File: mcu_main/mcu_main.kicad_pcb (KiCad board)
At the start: 2 copper layers, 108 x 61.7 mm, 55 parts, among them J1 Micro_SD_Card_Det_Hirose_DM3AT, J10 Conn_01x02_Pin, J2 Conn_01x10_Pin, J3 Conn_01x06_Pin, J4 4P4C_Shielded, J5 4P4C_Shielded, J6 Screw_Terminal_01x03_ebrake, J7 Screw_Terminal_01x03_throttle, J8 Screw_Terminal_01x06, J9 Conn_01x14_Socket, U1 ESP32-S3-WROOM-1, U2 USB_C_connector, U3 SGM2212-3.3, U4 VL53L1CXV0FY1, sw1 SW_Push_Dual, sw2 SW_Push_Dual

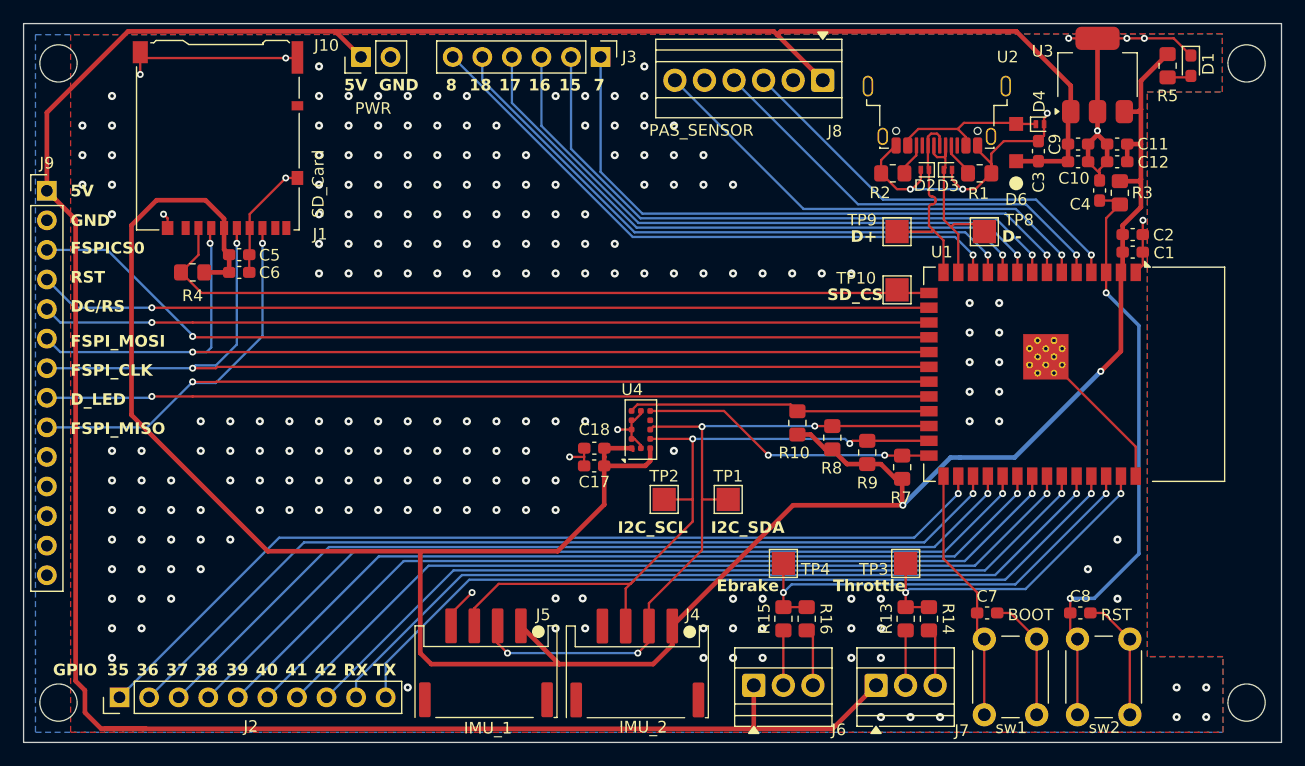
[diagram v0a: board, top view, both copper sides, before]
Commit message: fixed resistor values
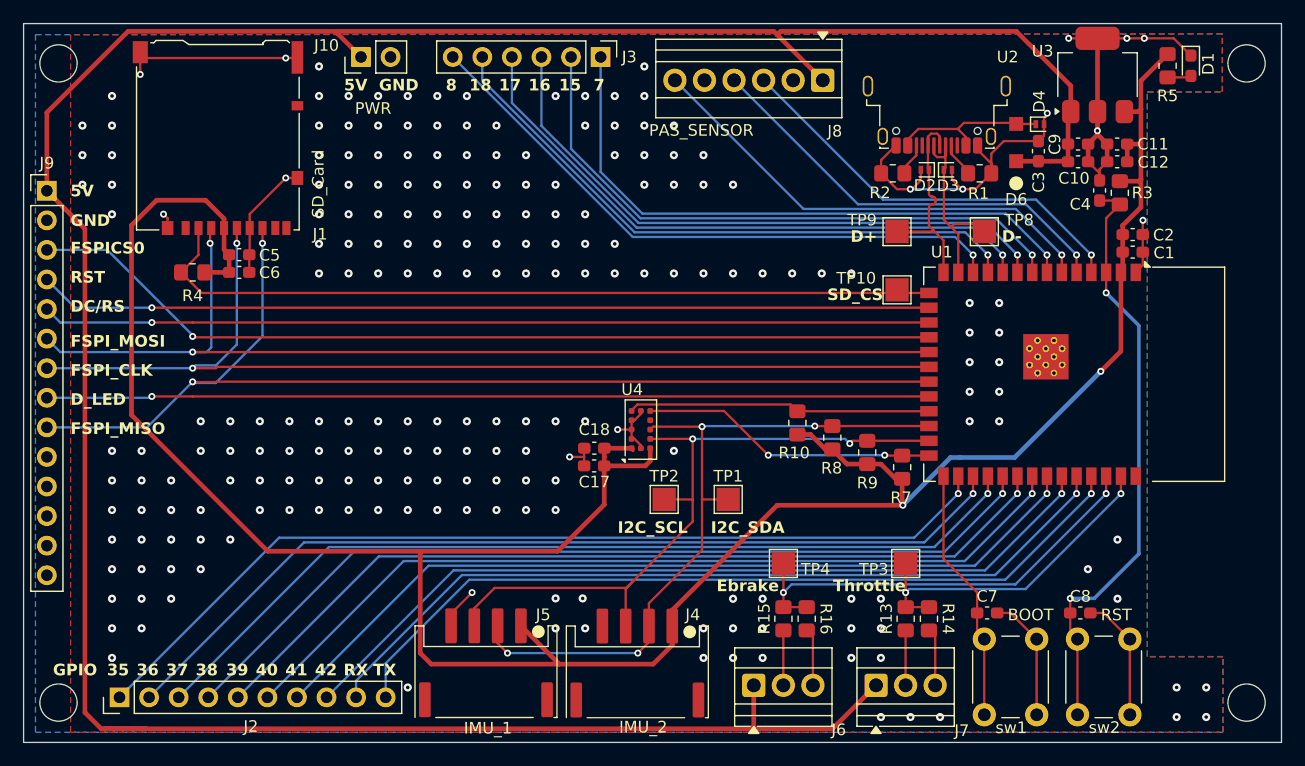
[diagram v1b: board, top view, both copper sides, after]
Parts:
- R10, R7: value 1.2K -> 10K
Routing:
- net GND: track 151.7 -> 138.2 mm
- net ESP_3v3: track 224.4 -> 225.2 mm
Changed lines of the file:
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@@
 			)
 		)
-		(property "Value" "1.2K"
+		(property "Value" "10K"
 			(at 0 1.65 90)
 			(layer "F.Fab")
@@
 			)
 		)
-		(property "Value" "1.2K"
+		(property "Value" "10K"
 			(at 0 1.65 90)
 			(layer "F.Fab")
@@
 	)
 	(segment
-		(start 187.8 98.62)
-		(end 195.52 106.34)
-		(width 0.2)
-		(layer "F.Cu")
-		(net 1)
-	)
-	(segment
 		(start 173.654168 82.862357)
 		(end 173.654168 81.723429)
@@
 	)
 	(segment
-		(start 195.52 106.34)
-		(end 195.52 108.87)
-		(width 0.2)
-		(layer "F.Cu")
-		(net 1)
-	)
-	(segment
 		(start 187.163225 80.095)
 		(end 184.191258 80.095)
@@
 	)
 	(segment
+		(start 175.52 111.37)
+		(end 164.72 111.37)
+		(width 0.4)
+		(layer "F.Cu")
+		(net 2)
+	)
+	(segment
+		(start 164.72 111.37)
+		(end 155.714177 120.375823)
+		(width 0.4)
+		(layer "F.Cu")
+		(net 2)
+	)
+	(segment
 		(start 115.52 91.37)
 		(end 117.6575 91.37)
@@
 	)
 	(segment
+		(start 155.714177 120.375823)
+		(end 155.714177 121.744314)
+		(width 0.4)
+		(layer "F.Cu")
+		(net 2)
+	)
+	(segment
 		(start 149.871933 106.464703)
 		(end 149.871933 107.219085)
@@
 	)
 	(segment
-		(start 166.088491 111.37)
-		(end 155.714177 121.744314)
-		(width 0.4)
-		(layer "F.Cu")
-		(net 2)
-	)
-	(segment
 		(start 195.97 85.765227)
 		(end 194.3975 87.337727)
@@
 	)
 	(segment
-		(start 175.52 111.37)
-		(end 166.088491 111.37)
-		(width 0.4)
-		(layer "F.Cu")
-		(net 2)
-	)
-	(segment
 		(start 117.22 89.4125)
 		(end 117.6575 89.85)
@@
 	)
 	(segment
-		(start 104.47 86.83)
-		(end 104.47 126.47)
-		(width 0.4)
-		(layer "F.Cu")
-		(net 3)
-	)
-	(segment
 		(start 185.251794 81.82)
 		(end 187.163225 81.82)
@@
 	)
 	(segment
-		(start 106.67 130.57)
-		(end 110.52 130.57)
-		(width 0.4)
-		(layer "F.Cu")
-		(net 3)
-	)
-	(segment
-		(start 105.27 129.17)
-		(end 106.67 130.57)
-		(width 0.4)
-		(layer "F.Cu")
-		(net 3)
-	)
-	(segment
 		(start 108.97 70.67)
 		(end 126.78 70.67)
@@
 	)
 	(segment
-		(start 104.47 126.47)
-		(end 105.27 127.27)
-		(width 0.4)
-		(layer "F.Cu")
-		(net 3)
-	)
-	(segment
 		(start 102 77.64)
 		(end 108.97 70.67)
@@
 	)
 	(segment
-		(start 105.27 127.27)
-		(end 105.27 129.17)
+		(start 105.27 129.17)
+		(end 106.67 130.57)
 		(width 0.4)
 		(layer "F.Cu")
@@
 	)
 	(segment
-		(start 102 84.36)
-		(end 104.47 86.83)
+		(start 105.27 87.63)
+		(end 105.27 129.17)
+		(width 0.4)
+		(layer "F.Cu")
+		(net 3)
+	)
+	(segment
+		(start 106.67 130.57)
+		(end 110.52 130.57)
 		(width 0.4)
 		(layer "F.Cu")
@@
 	)
 	(segment
+		(start 102 84.36)
+		(end 105.27 87.63)
+		(width 0.4)
+		(layer "F.Cu")
+		(net 3)
+	)
+	(segment
 		(start 126.78 70.67)
 		(end 164.44 70.67)
@@
 	)
 	(segment
-		(start 191.71 110.37)
-		(end 184.312859 117.767141)
+		(start 131.1 124.94)
+		(end 131.1 127.87)
 		(width 0.2)
 		(layer "B.Cu")
@@
 	)
 	(segment
-		(start 131.1 124.94)
-		(end 131.1 127.87)
+		(start 191.71 110.37)
+		(end 184.312859 117.767141)
 		(width 0.2)
 		(layer "B.Cu")
@@
 	)
 	(segment
+		(start 154.07 104.62)
+		(end 153.82 104.87)
+		(width 0.2)
+		(layer "F.Cu")
+		(net 32)
+	)
+	(segment
 		(start 153.71 123.12)
 		(end 152.76 124.07)
@@
 	)
 	(segment
-		(start 154.07 104.62)
-		(end 153.82 104.87)
-		(width 0.2)
-		(layer "F.Cu")
-		(net 32)
-	)
-	(segment
-		(start 158.27 104.62)
-		(end 154.07 104.62)
+		(start 169.46 104.57)
+		(end 167.96 104.57)
 		(width 0.2)
 		(layer "F.Cu")
@@
 	)
 	(segment
-		(start 169.46 104.57)
-		(end 167.96 104.57)
+		(start 158.27 115.22)
+		(end 153.71 119.78)
 		(width 0.2)
 		(layer "F.Cu")
@@
 	)
 	(segment
-		(start 158.27 115.22)
-		(end 153.71 119.78)
+		(start 158.27 104.62)
+		(end 154.07 104.62)
 		(width 0.2)
 		(layer "F.Cu")
@@
 	)
 	(segment
-		(start 140.810001 118.12)
-		(end 152.12 118.12)
+		(start 157.47 105.67)
+		(end 153.82 105.67)
 		(width 0.2)
 		(layer "F.Cu")
@@
 	)
 	(segment
-		(start 157.47 105.67)
-		(end 153.82 105.67)
+		(start 138.71 120.220001)
+		(end 140.460001 118.47)
 		(width 0.2)
 		(layer "F.Cu")
@@
 	)
 	(segment
-		(start 138.71 121.72)
-		(end 138.71 120.220001)
+		(start 151.77 118.47)
+		(end 152.445 117.795)
 		(width 0.2)
 		(layer "F.Cu")
@@
 	)
 	(segment
+		(start 140.460001 118.47)
+		(end 151.77 118.47)
+		(width 0.2)
+		(layer "F.Cu")
+		(net 33)
+	)
+	(segment
 		(start 157.47 112.77)
 		(end 152.445 117.795)
@@
 	)
 	(segment
-		(start 138.71 120.220001)
-		(end 140.810001 118.12)
-		(width 0.2)
-		(layer "F.Cu")
-		(net 33)
-	)
-	(segment
-		(start 152.12 118.12)
-		(end 152.445 117.795)
+		(start 138.71 121.72)
+		(end 138.71 120.220001)
 		(width 0.2)
 		(layer "F.Cu")
@@
 	)
 	(segment
+		(start 163.96 107.07)
+		(end 160.16 103.27)
+		(width 0.2)
+		(layer "F.Cu")
+		(net 51)
+	)
+	(segment
 		(start 175.46 107.105)
 		(end 173.995 107.105)
@@
 		(width 0.2)
 		(layer "F.Cu")
-		(net 51)
-	)
-	(segment
-		(start 163.96 107.07)
-		(end 160.16 103.27)
-		(width 0.2)
-		(layer "F.Cu")

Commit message: pushing final changes
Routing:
- net GND: vias 224 -> 219

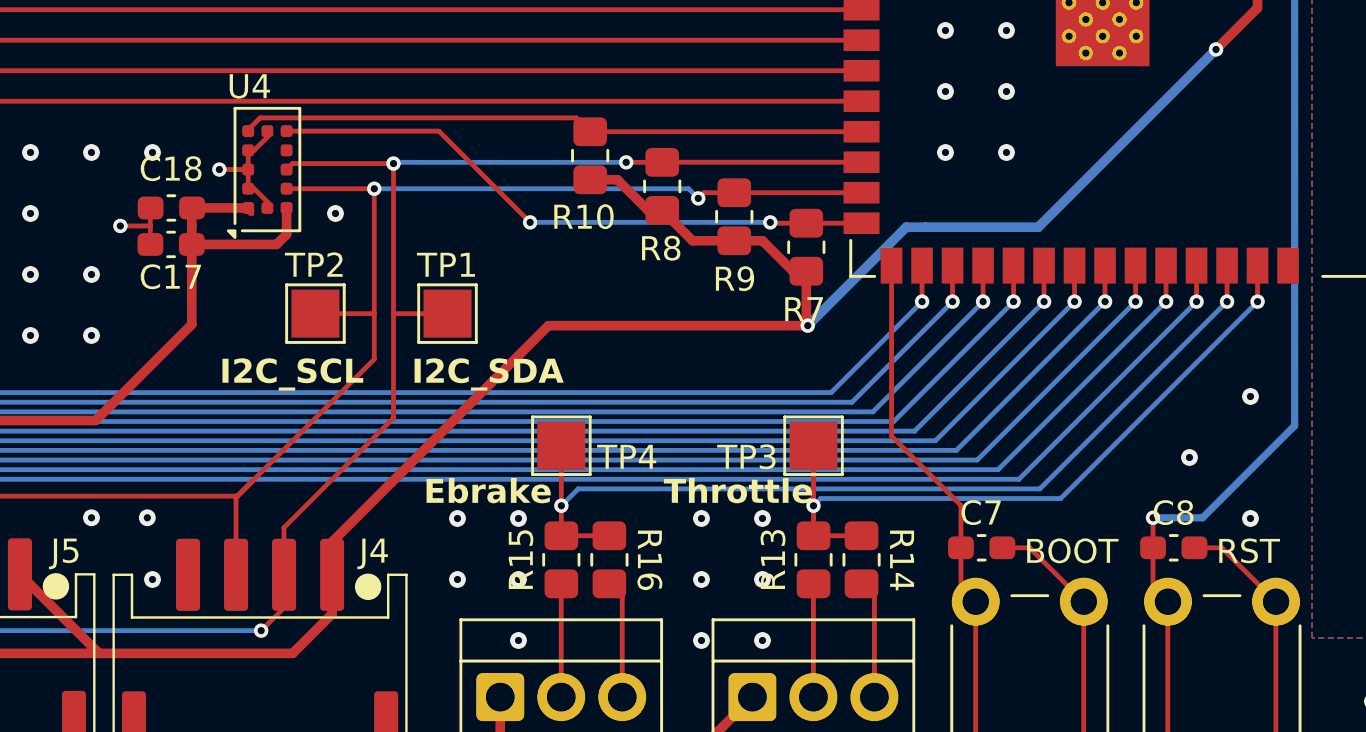
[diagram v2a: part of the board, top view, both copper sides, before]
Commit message: edited some vias that were on the silcscreen
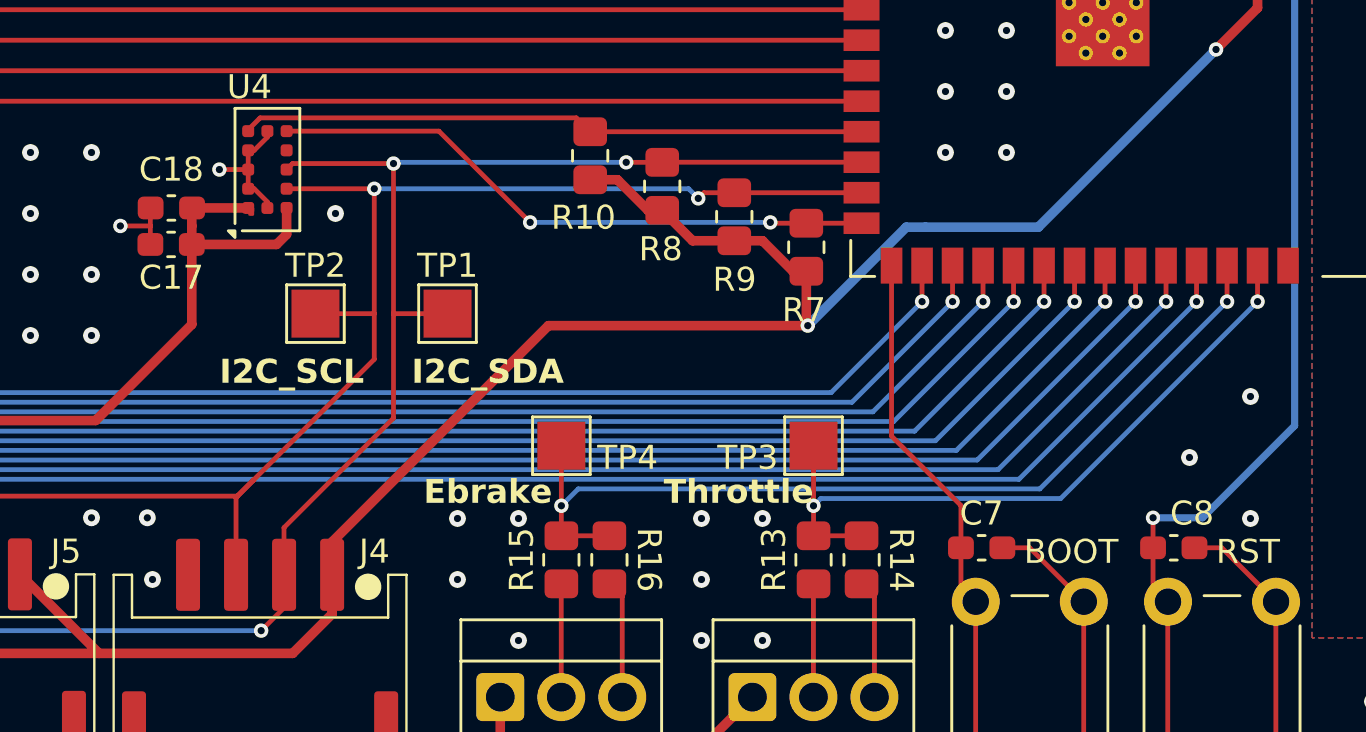
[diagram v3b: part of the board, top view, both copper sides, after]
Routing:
- net GND: vias 219 -> 216
